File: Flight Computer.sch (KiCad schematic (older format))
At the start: 25 parts, among them J1 Conn_01x08, U1 VXO7803-1000, U2 W25Q32JVSS, U3 W25Q32JVSS, U4 Adafruit_GPS_THT, U5 ADXL343, U8 BMP280

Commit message: Updated pinmap Added USART3 for external communication
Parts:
- U2, U3: value W25Q32JVSS -> W25Q16JVSS
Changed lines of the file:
@@
 P 2750 4800
 F 0 "U2" H 2400 5150 50  0000 C CNN
-F 1 "W25Q32JVSS" H 3050 5150 50  0000 C CNN
+F 1 "W25Q16JVSS" H 3050 5150 50  0000 C CNN
 F 2 "Package_SO:SOIC-8_5.23x5.23mm_P1.27mm" H 2750 4800 50  0001 C CNN
 F 3 "http://www.winbond.com/resource-files/w25q32jv%20revg%2003272018%20plus.pdf" H 2750 4800 50  0001 C CNN
@@
 P 4850 4800
 F 0 "U3" H 4500 5150 50  0000 C CNN
-F 1 "W25Q32JVSS" H 5150 5150 50  0000 C CNN
+F 1 "W25Q16JVSS" H 5150 5150 50  0000 C CNN
 F 2 "Package_SO:SOIC-8_5.23x5.23mm_P1.27mm" H 4850 4800 50  0001 C CNN
 F 3 "http://www.winbond.com/resource-files/w25q32jv%20revg%2003272018%20plus.pdf" H 4850 4800 50  0001 C CNN

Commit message: Cleaned up libraries Changed ADXL345 footprint
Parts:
- U5: value ADXL343 -> ADXL345; footprint Package_LGA:LGA-14_3x5mm_P0.8mm_LayoutBorder1x6y -> SamacSys_Parts:CC-14-1
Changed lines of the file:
@@
 EESchema Schematic File Version 4
-LIBS:Flight Computer-cache
 EELAYER 30 0
 EELAYER END
@@
 P 5200 1500
 F 0 "U5" H 5744 1546 50  0000 L CNN
-F 1 "ADXL343" H 5744 1455 50  0000 L CNN
-F 2 "Package_LGA:LGA-14_3x5mm_P0.8mm_LayoutBorder1x6y" H 5200 1500 50  0001 C CNN
+F 1 "ADXL345" H 5744 1455 50  0000 L CNN
+F 2 "SamacSys_Parts:CC-14-1" H 5200 1500 50  0001 C CNN
 F 3 "https://www.analog.com/media/en/technical-documentation/data-sheets/ADXL343.pdf" H 5200 1500 50  0001 C CNN
 	1    5200 1500

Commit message: Adding test points
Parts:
- added TP?: B+, TestPoint:TestPoint_Pad_D1.0mm, symbol Connector:TestPoint
- added TP?: 3V3, TestPoint:TestPoint_Pad_D1.0mm, symbol Connector:TestPoint
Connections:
- net labels removed: ADC3, ADC4, I2C1_SCL, I2C1_SDA
- no-connect marks 32 -> 30
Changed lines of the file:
@@
 F10 "USART1_TX" B R 4150 6500 60
 F11 "USART1_RX" B R 4150 6600 60
-F12 "I2C1_SDA" B L 2450 6400 60
-F13 "I2C1_SCL" B L 2450 6500 60
-F14 "SPI2_CS1" B L 2450 7000 60
-F15 "SPI2_CS2" B L 2450 7100 60
-F16 "SPI2_SCK" B L 2450 6700 60
-F17 "SPI2_MISO" B L 2450 6800 60
-F18 "SPI2_MOSI" B L 2450 6900 60
-F19 "SPI1_SCK" B R 4150 7000 60
-F20 "SPI1_MISO" B R 4150 7100 60
-F21 "SPI1_MOSI" B R 4150 7200 60
-F22 "SPI1_CS1" B R 4150 7300 60
-F23 "SPI1_CS2" B R 4150 7400 60
-F24 "SPI1_CS3" B R 4150 7500 60
-F25 "SPI1_CS4" B R 4150 7600 60
-F26 "ADC1" B L 2450 7300 60
-F27 "ADC2" B L 2450 7400 60
-F28 "ADC3" B L 2450 7500 60
-F29 "ADC4" B L 2450 7600 60
+F12 "SPI2_CS1" B L 2450 7000 60
+F13 "SPI2_CS2" B L 2450 7100 60
+F14 "SPI2_SCK" B L 2450 6700 60
+F15 "SPI2_MISO" B L 2450 6800 60
+F16 "SPI2_MOSI" B L 2450 6900 60
+F17 "SPI1_SCK" B R 4150 7000 60
+F18 "SPI1_MISO" B R 4150 7100 60
+F19 "SPI1_MOSI" B R 4150 7200 60
+F20 "SPI1_CS1" B R 4150 7300 60
+F21 "SPI1_CS2" B R 4150 7400 60
+F22 "SPI1_CS3" B R 4150 7500 60
+F23 "SPI1_CS4" B R 4150 7600 60
+F24 "ADC1" B L 2450 7300 60
+F25 "ADC2" B L 2450 7400 60
 $EndSheet
-NoConn ~ 1550 6400
-NoConn ~ 1550 6500
-Text Label 1600 6400 0    60   ~ 0
-I2C1_SDA
-Text Label 1600 6500 0    60   ~ 0
-I2C1_SCL
-Wire Wire Line
-	1550 6400 2450 6400
-Wire Wire Line
-	1550 6500 2450 6500
 Wire Wire Line
 	2450 6700 1550 6700
@@
 Wire Wire Line
 	2450 7400 1550 7400
-Wire Wire Line
-	2450 7500 1550 7500
-Wire Wire Line
-	2450 7600 1550 7600
 Text Label 1600 7300 0    60   ~ 0
 ADC1
 Text Label 1600 7400 0    60   ~ 0
 ADC2
-Text Label 1600 7500 0    60   ~ 0
-ADC3
-Text Label 1600 7600 0    60   ~ 0
-ADC4
 Text Label 1600 6700 0    60   ~ 0
 SPI2_SCK
@@
 	1450 7300 1000 7300
 Wire Bus Line
-	1450 7800 1000 7800
+	1450 7600 1000 7600
 Wire Bus Line
 	4850 7800 5500 7800
-Wire Bus Line
-	4850 7000 5500 7000
 Wire Bus Line
 	4850 6500 5500 6500
 Text Label 1050 7300 0    60   ~ 12
 SPI2
-Text Label 1050 7800 0    60   ~ 12
+Text Label 1050 7600 0    60   ~ 12
 ADC
 Text Label 4900 7800 0    60   ~ 12
@@
 	2200 1000 2200 950
 Wire Wire Line
-	2200 950  1750 950
+	2200 950  2000 950
 Connection ~ 1750 950
 Wire Wire Line
@@
 Wire Wire Line
 	7150 3750 7150 3850
+$Comp
+L Connector:TestPoint TP?
+U 1 1 5E1DD36B
+P 650 850
+F 0 "TP?" H 708 968 50  0000 L CNN
+F 1 "B+" H 708 877 50  0000 L CNN
+F 2 "TestPoint:TestPoint_Pad_D1.0mm" H 850 850 50  0001 C CNN
+F 3 "~" H 850 850 50  0001 C CNN
+	1    650  850
+	1    0    0    -1
+$EndComp
+$Comp
+L Connector:TestPoint TP?
+U 1 1 5E1E7CDF
+P 2000 800
+F 0 "TP?" H 2058 918 50  0000 L CNN
+F 1 "3V3" H 2058 827 50  0000 L CNN
+F 2 "TestPoint:TestPoint_Pad_D1.0mm" H 2200 800 50  0001 C CNN
+F 3 "~" H 2200 800 50  0001 C CNN
+	1    2000 800
+	1    0    0    -1
+$EndComp
+Wire Wire Line
+	650  850  650  950
+Wire Wire Line
+	650  950  950  950
+Wire Wire Line
+	2000 800  2000 950
+Connection ~ 2000 950
+Wire Wire Line
+	2000 950  1750 950
+Wire Bus Line
+	4850 7000 5500 7000
 Wire Bus Line
 	7400 5650 7400 6350
@@
 	850  2300 850  3300
 Wire Bus Line
-	1450 7400 1450 7800
+	1450 7400 1450 7600
 Wire Bus Line
 	6350 2650 6350 3350

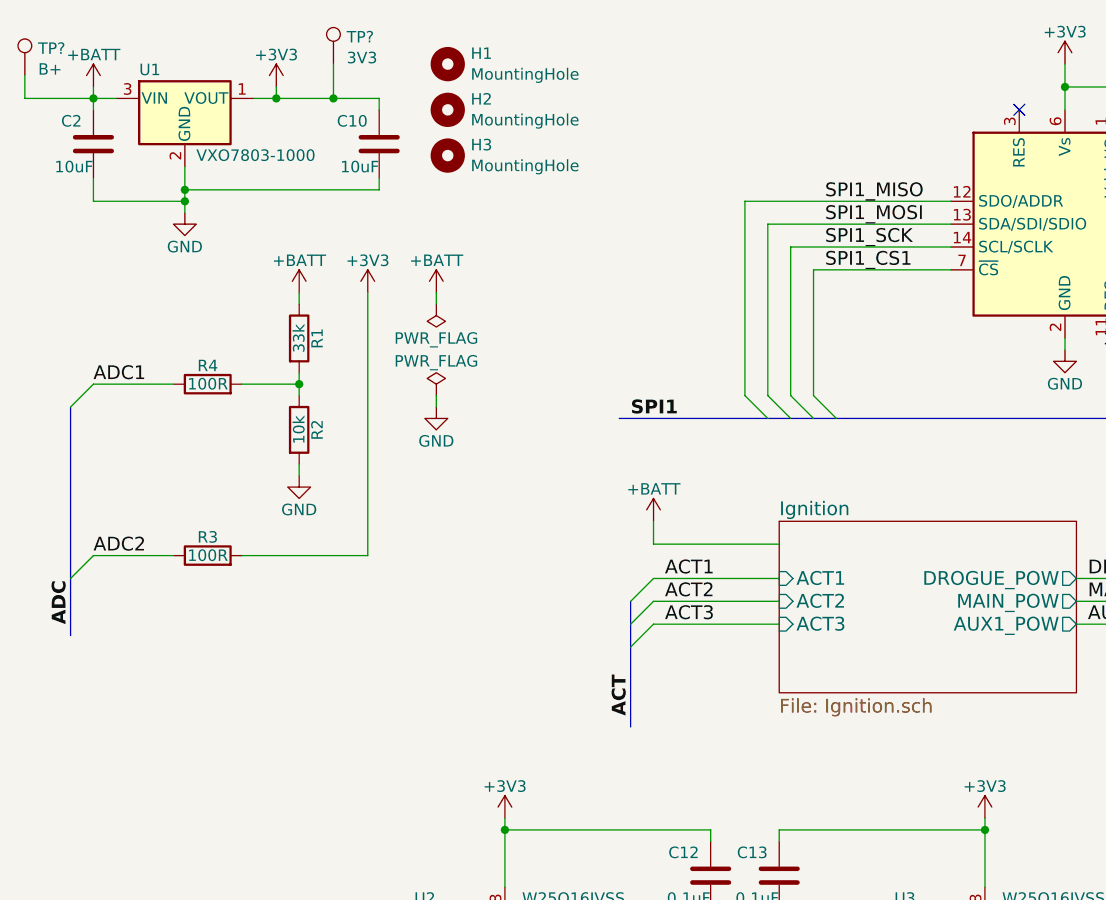
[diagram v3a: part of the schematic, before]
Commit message: Finished adding test points Schematic annotated
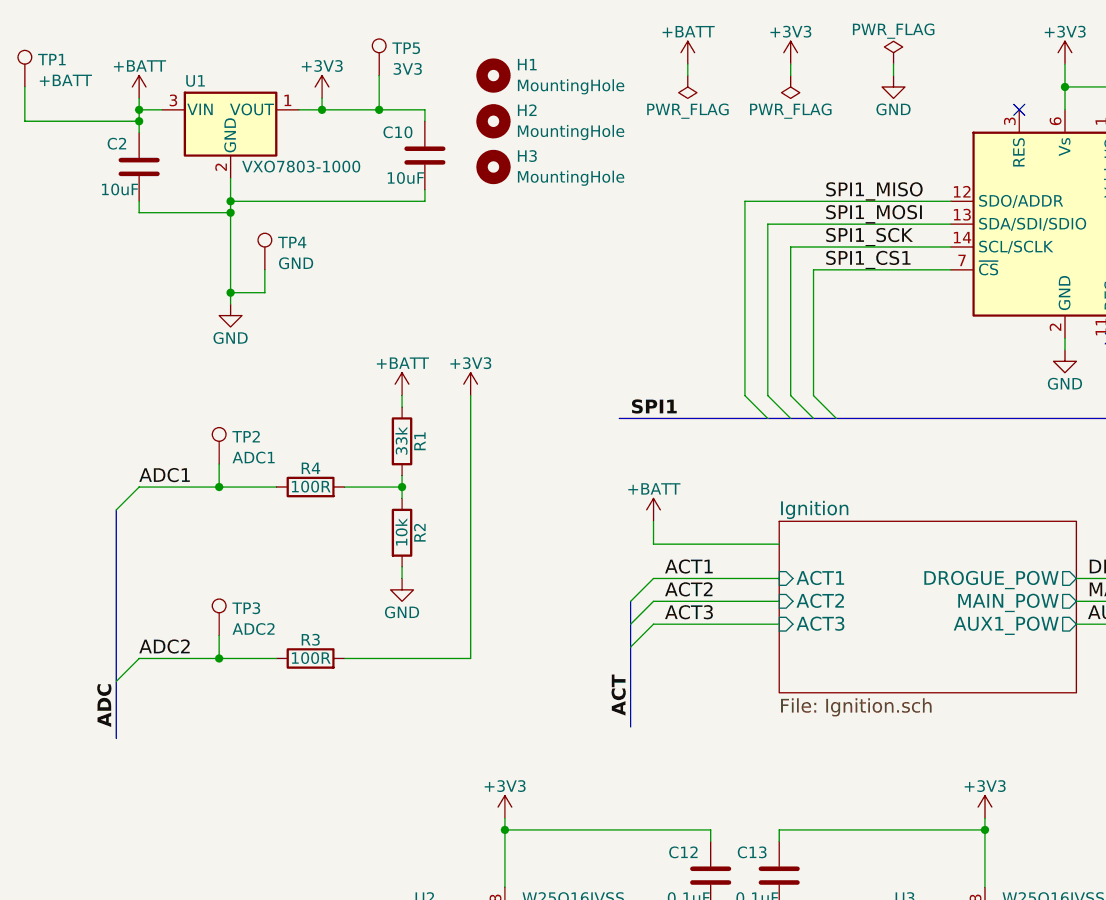
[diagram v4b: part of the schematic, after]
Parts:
- added TP2: ADC1, TestPoint:TestPoint_Pad_D1.0mm, symbol Connector:TestPoint
- added TP3: ADC2, TestPoint:TestPoint_Pad_D1.0mm, symbol Connector:TestPoint
- added TP4: GND, TestPoint:TestPoint_Pad_D1.0mm, symbol Connector:TestPoint
- TP1: renamed from TP?; value B+ -> +BATT
- gave numbers to parts that had none: 1
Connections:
- wire segments 161 -> 170
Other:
- moved on the sheet: C10, C2, H1, H2, H3, R1, R2, R3, R4, TP1, TP5, U1

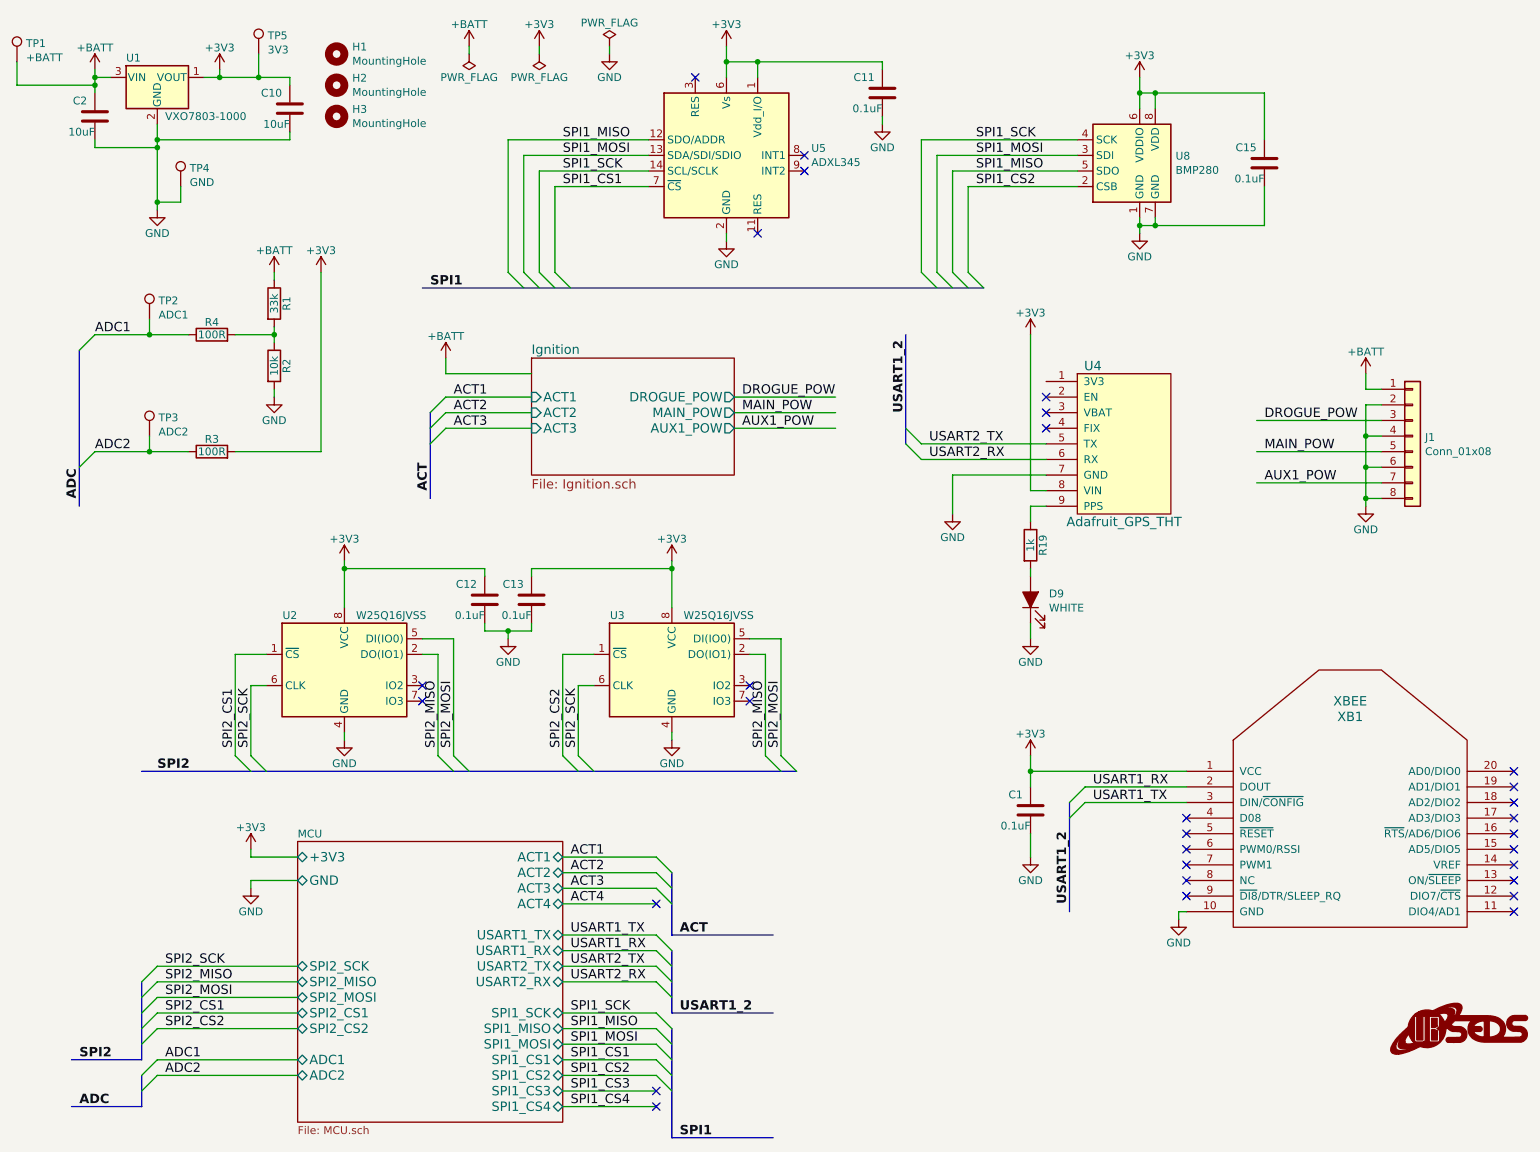
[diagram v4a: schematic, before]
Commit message: Added 10R series termination resistors to high-speed digital lines Added reverse-power protection diode Added ADC filter capacitors Added I2C pullups Added individual polyfuses to pyro drivers Changed UBSEDS logo to smaller variant Reduced LED resistors to 470R Reduced most SMD footprints to 0603 Minor schematic cleanup
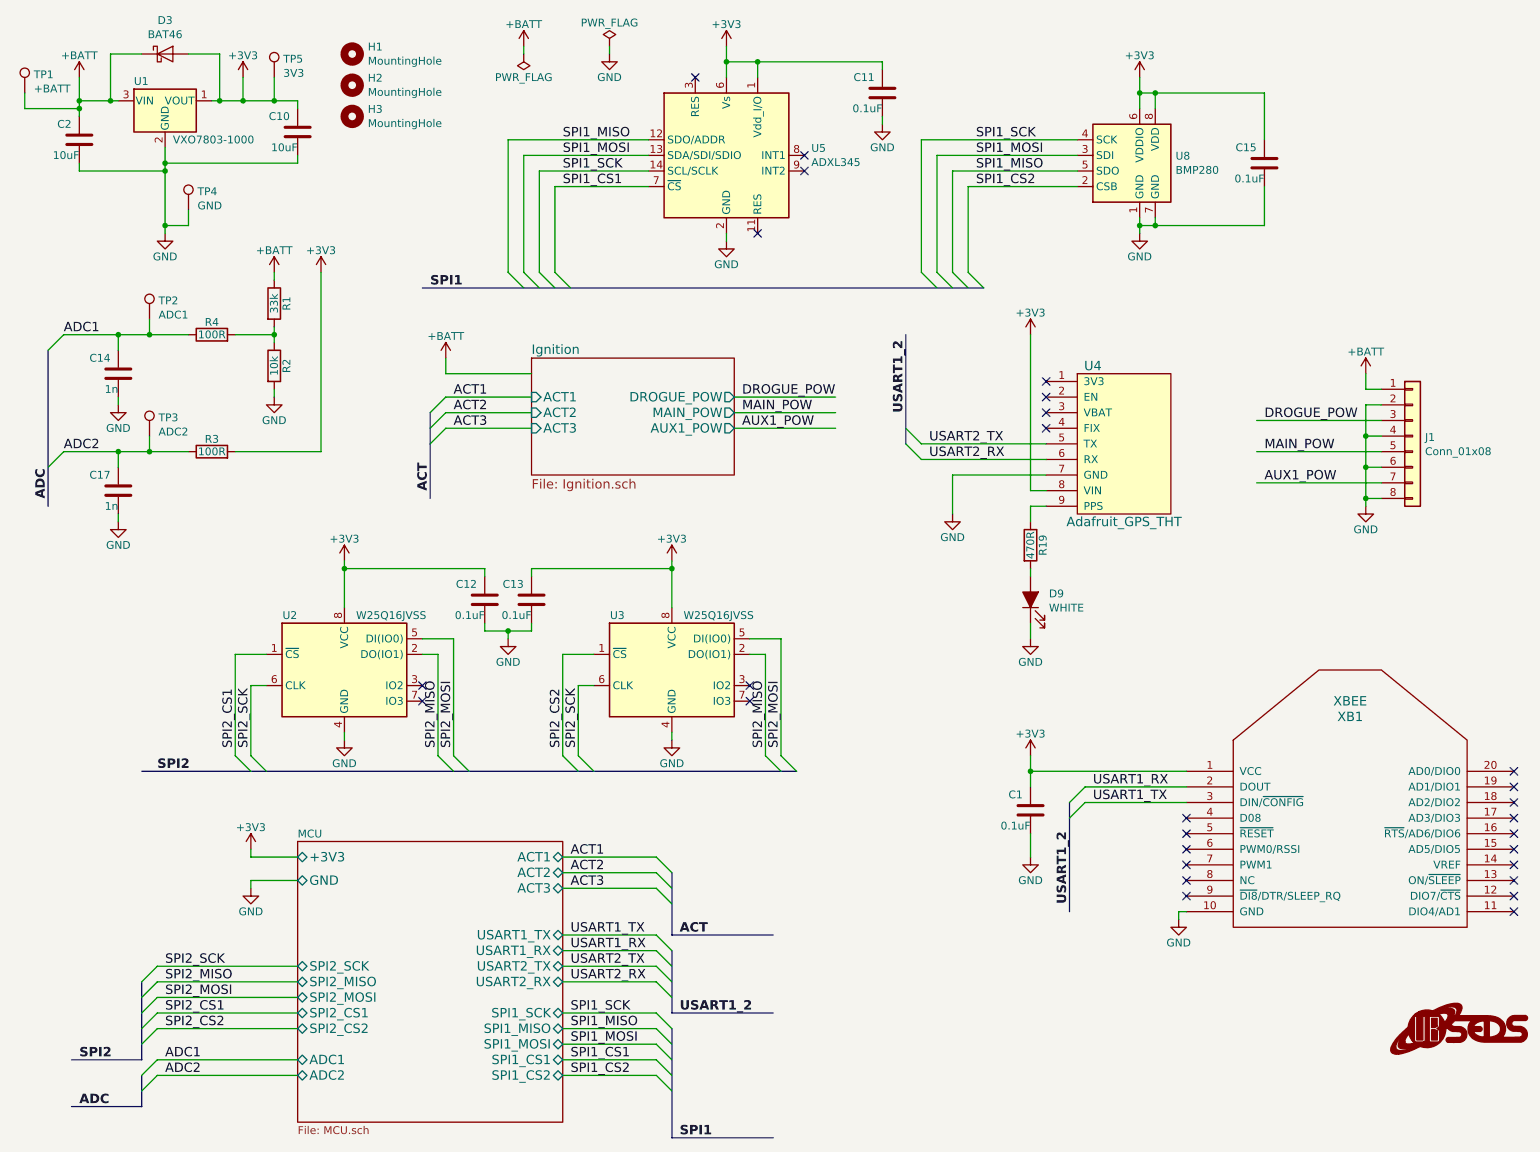
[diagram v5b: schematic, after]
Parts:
- added C14, C17: 1n, Capacitor_SMD:C_0603_1608Metric_Pad1.05x0.95mm_HandSolder, symbol Device:C
- added D3: BAT46, Diode_THT:D_DO-35_SOD27_P7.62mm_Horizontal, symbol Diode:BAT46
- G1: footprint Flight-Computer:UB-SEDS-Logo -> Flight-Computer:SEDS_logo_soldermask
- R1, R2, R3, R4: footprint Resistor_SMD:R_1206_3216Metric_Pad1.42x1.75mm_HandSolder -> Resistor_SMD:R_0603_1608Metric_Pad1.05x0.95mm_HandSolder
- R19: value 1k -> 470R; footprint Resistor_SMD:R_1206_3216Metric_Pad1.42x1.75mm_HandSolder -> Resistor_SMD:R_0603_1608Metric_Pad1.05x0.95mm_HandSolder
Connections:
- net labels removed: ACT4, SPI1_CS3, SPI1_CS4
- wire segments 170 -> 178
- no-connect marks 30 -> 28
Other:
- moved on the sheet: C10, C2, H1, H2, H3, TP1, TP4, TP5, U1

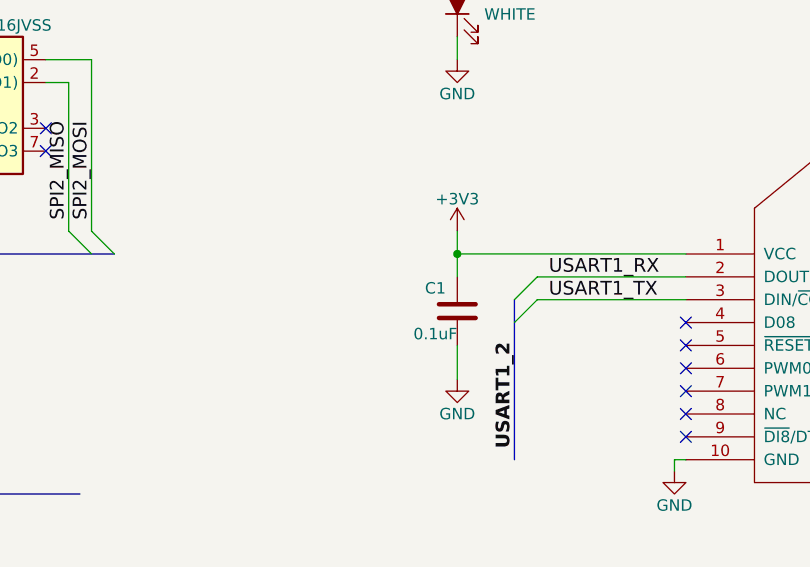
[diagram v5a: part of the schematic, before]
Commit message: Fixed silk Fixed JTAG Added PAYLOAD connector with I2C
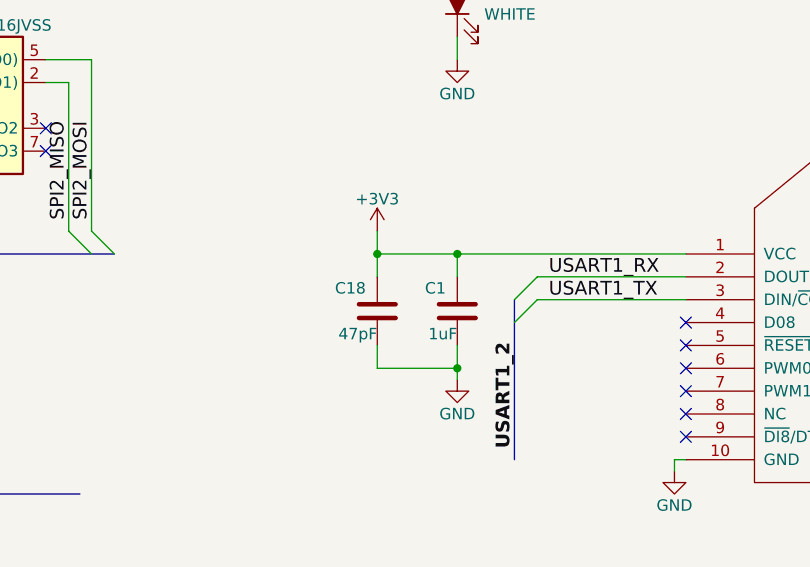
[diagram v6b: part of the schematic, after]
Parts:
- added C18: 47pF, Capacitor_SMD:C_0603_1608Metric_Pad1.05x0.95mm_HandSolder, symbol Device:C
- C1: value 0.1uF -> 1uF
- D3: footprint Diode_THT:D_DO-35_SOD27_P7.62mm_Horizontal -> Diode_SMD:D_SOD-123
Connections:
- wire segments 178 -> 183
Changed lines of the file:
@@
 P 7150 5700
 F 0 "C1" H 7200 5600 50  0000 L CNN
-F 1 "0.1uF" H 7150 5800 50  0000 L CNN
+F 1 "1uF" H 7150 5800 50  0000 L CNN
 F 2 "Capacitor_SMD:C_0603_1608Metric_Pad1.05x0.95mm_HandSolder" H 7188 5550 50  0001 C CNN
 F 3 "" H 7150 5700 50  0001 C CNN
@@
 L power:+3V3 #PWR018
 U 1 1 5AD7F258
-P 7150 5350
-F 0 "#PWR018" H 7150 5200 50  0001 C CNN
-F 1 "+3V3" H 7150 5490 50  0000 C CNN
-F 2 "" H 7150 5350 50  0001 C CNN
-F 3 "" H 7150 5350 50  0001 C CNN
-	1    7150 5350
-	1    0    0    -1
-$EndComp
-Wire Wire Line
-	7150 5450 7150 5350
+P 6800 5350
+F 0 "#PWR018" H 6800 5200 50  0001 C CNN
+F 1 "+3V3" H 6800 5490 50  0000 C CNN
+F 2 "" H 6800 5350 50  0001 C CNN
+F 3 "" H 6800 5350 50  0001 C CNN
+	1    6800 5350
+	1    0    0    -1
+$EndComp
 Wire Wire Line
 	2300 2250 2300 2300
@@
 	1600 1550 1600 1600
 Wire Wire Line
-	7150 5850 7150 6000
-Connection ~ 7150 5450
+	7150 5850 7150 5950
 Wire Wire Line
 	7150 5450 8150 5450
@@
 F 0 "D3" H 1600 1066 50  0000 C CNN
 F 1 "BAT46" H 1600 975 50  0000 C CNN
-F 2 "Diode_THT:D_DO-35_SOD27_P7.62mm_Horizontal" H 1600 675 50  0001 C CNN
+F 2 "Diode_SMD:D_SOD-123" H 1600 675 50  0001 C CNN
 F 3 "http://www.vishay.com/docs/85662/bat46.pdf" H 1600 850 50  0001 C CNN
 	1    1600 850
@@
 	1    0    0    -1
 $EndComp
+$Comp
+L Device:C C18
+U 1 1 5E3A4682
+P 6800 5700
+F 0 "C18" H 6850 5600 50  0000 L CNN
+F 1 "47pF" H 6800 5800 50  0000 L CNN
+F 2 "Capacitor_SMD:C_0603_1608Metric_Pad1.05x0.95mm_HandSolder" H 6838 5550 50  0001 C CNN
+F 3 "" H 6800 5700 50  0001 C CNN
+	1    6800 5700
+	-1   0    0    1
+$EndComp
+Wire Wire Line
+	6800 5350 6800 5450
+Wire Wire Line
+	6800 5450 7150 5450
+Connection ~ 7150 5450
+Wire Wire Line
+	6800 5450 6800 5550
+Connection ~ 6800 5450
+Wire Wire Line
+	6800 5850 6800 5950
+Wire Wire Line
+	6800 5950 7150 5950
 Wire Bus Line
 	7400 5650 7400 6350
@@
 Wire Bus Line
 	3250 2350 6850 2350
+Connection ~ 7150 5950
+Wire Wire Line
+	7150 5950 7150 6000
 $EndSCHEMATC
